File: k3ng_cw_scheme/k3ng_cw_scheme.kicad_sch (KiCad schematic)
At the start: 32 parts, among them J1 INPUT KEY, J2 OUTPUT KEY/PTT, SW1 CMD, SW2 MEM1, SW3 MEM2, SW4 MEM3, SW5 MEM4, U1 PC817, U2 PC817

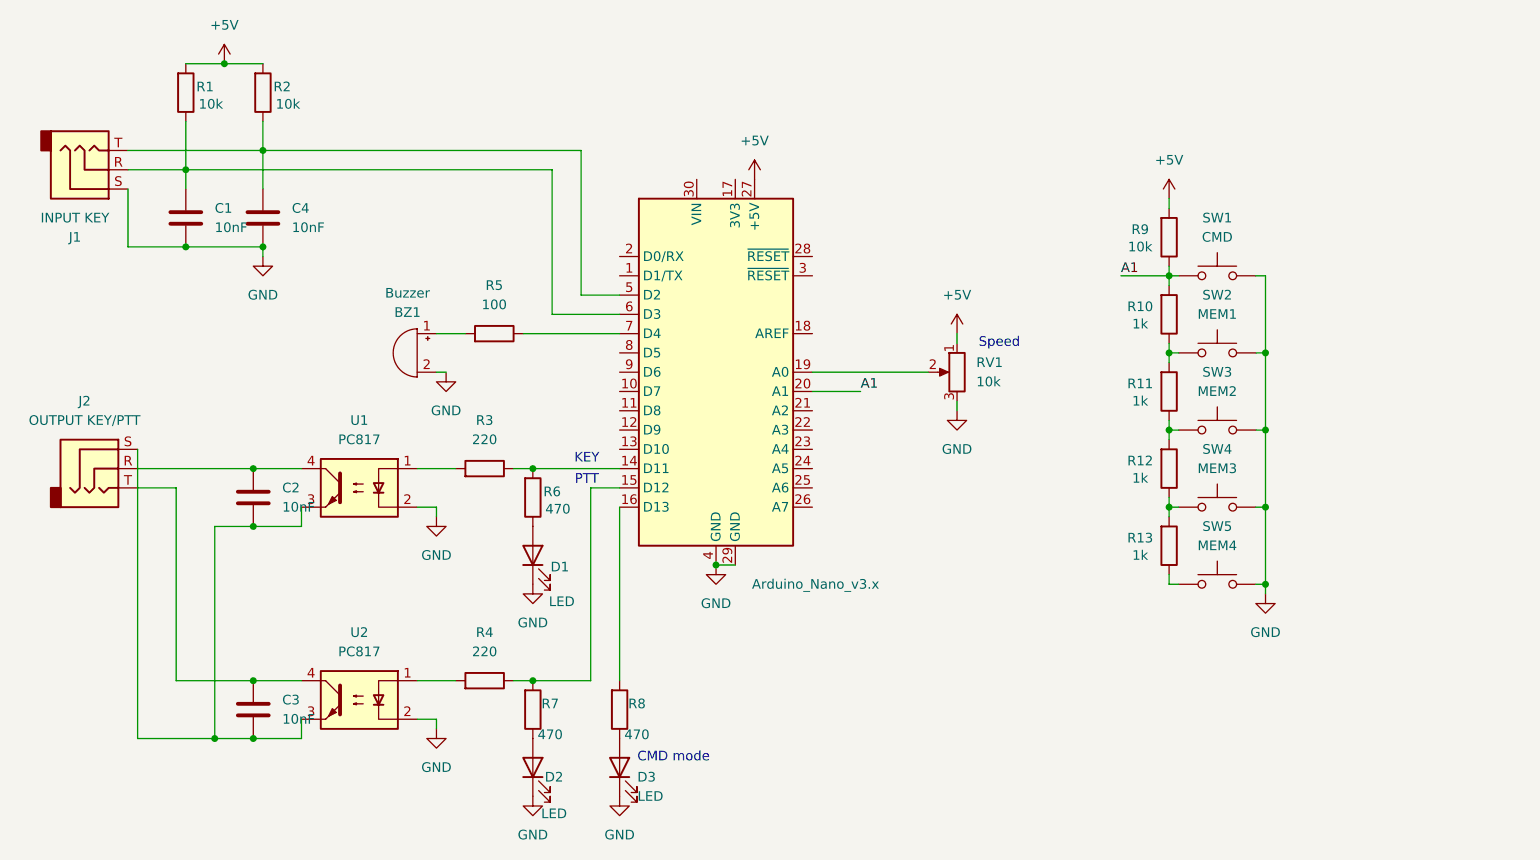
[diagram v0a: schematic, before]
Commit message: Add keyboard connector Start working on PCB
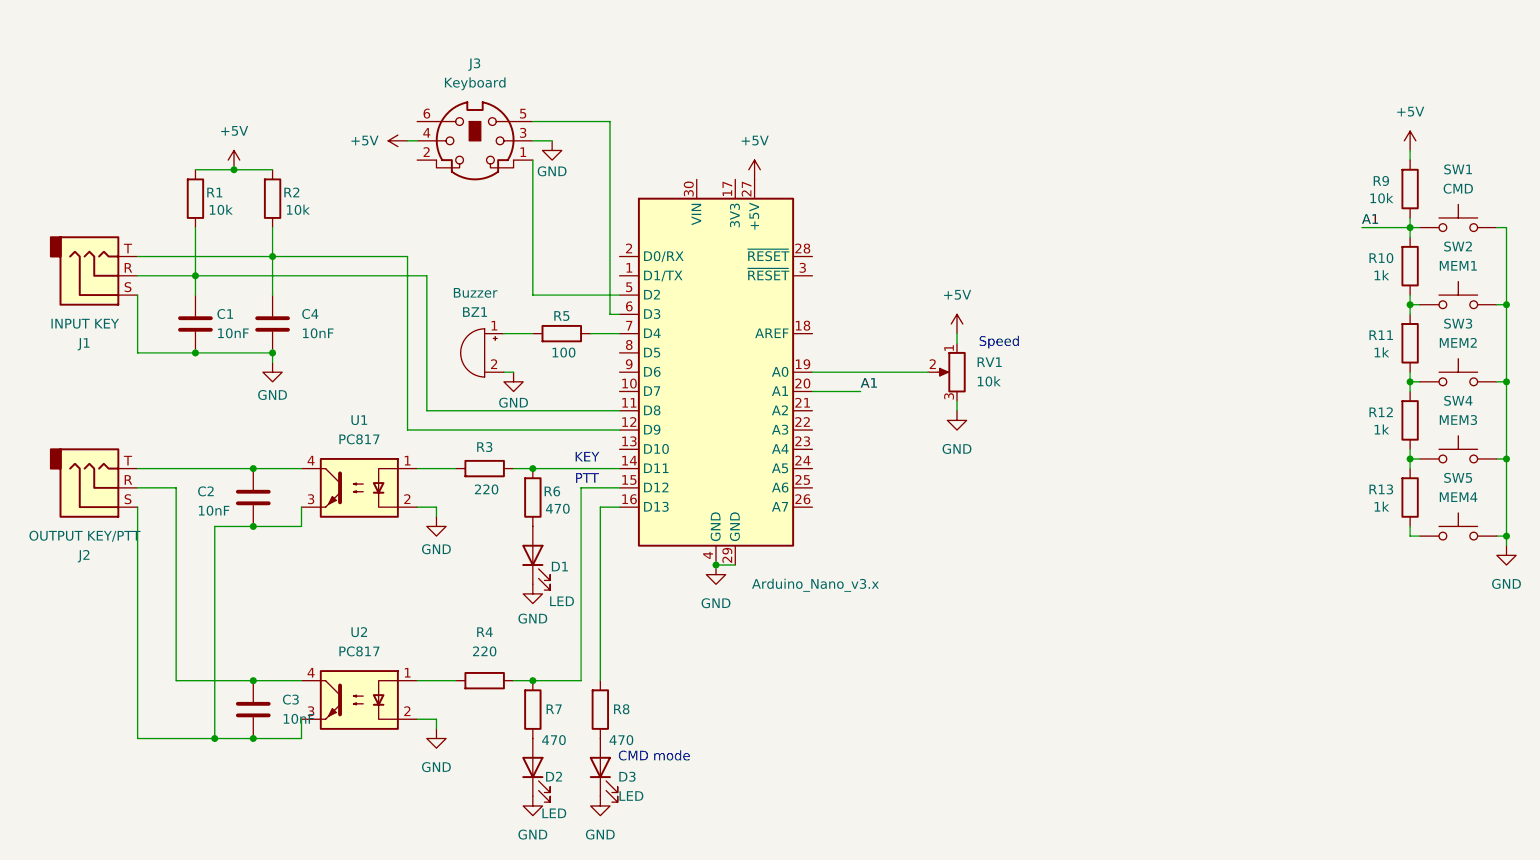
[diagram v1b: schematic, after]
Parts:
- added J3: Keyboard, Footprints:Connector_Mini-DIN_Female_6Pin_2rows, symbol Connector:Mini-DIN-6
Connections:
- net +5V: now also J3.4
- net GND: now also J3.3
- net at C2.1, U1.4: now also J2.T; no longer J2.R
- net at C4.1, J1.T, R2.1: now also A1.12 (D9); no longer A1.5 (D2)
- net at C3.1, U2.4: now also J2.R; no longer J2.T
- net at C1.1, J1.R, R1.1: now also A1.11 (D8); no longer A1.6 (D3)
- new net: A1.5 (D2), J3.1
- new net: A1.6 (D3), J3.5
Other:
- moved on the sheet: BZ1, C1, C4, D3, J1, J2, R1, R10, R11, R12, R13, R2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

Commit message: Add scheme to pdf
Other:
- company: (none) -> R1TBJ
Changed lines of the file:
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@@
 	(generator_version "9.0")
 	(paper "A4")
+	(title_block
+		(company "R1TBJ")
+	)
 	(text "KEY"
 		(exclude_from_sim no)
